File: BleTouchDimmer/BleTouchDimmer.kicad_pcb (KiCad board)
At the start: 2 copper layers, 10 parts, among them SW1 SW_PUSH, U2 MDBT40, Y2 Crystal

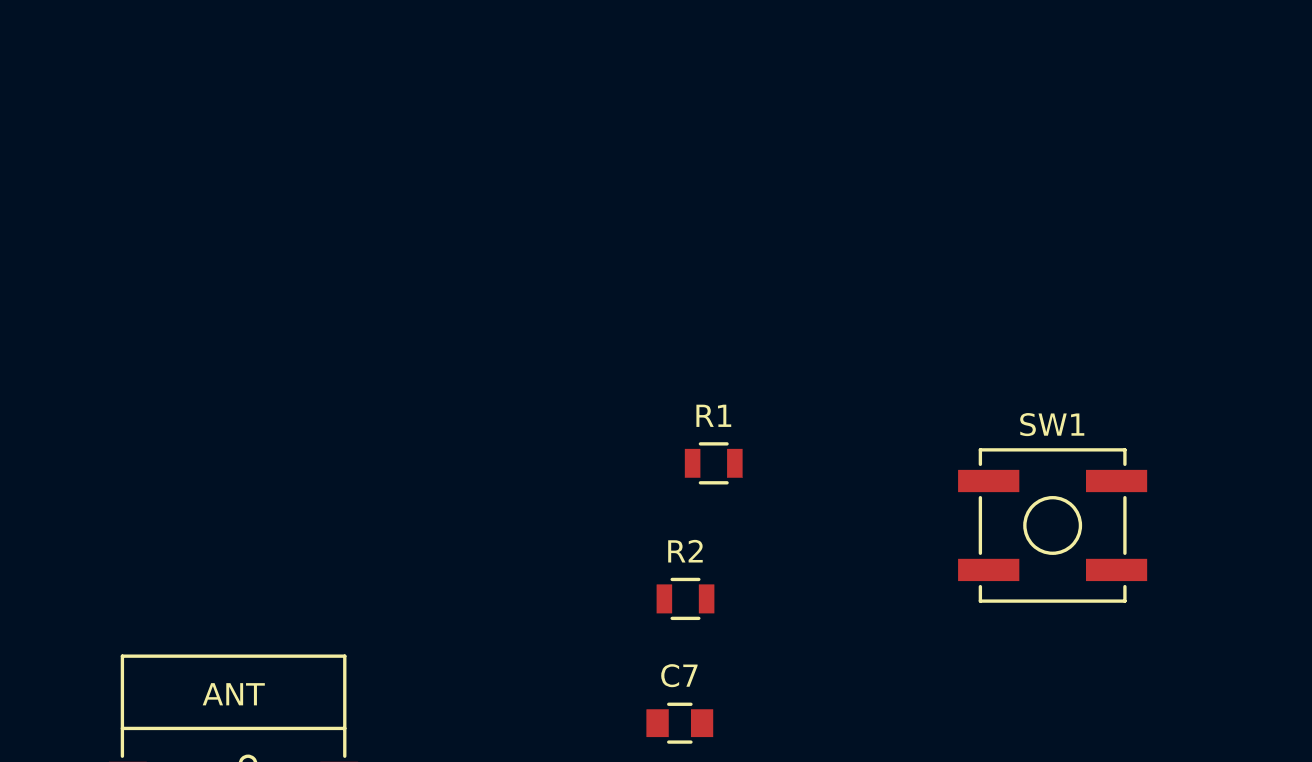
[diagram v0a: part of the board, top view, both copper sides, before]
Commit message: Started ZC_detect part. TODO select optoisolator.
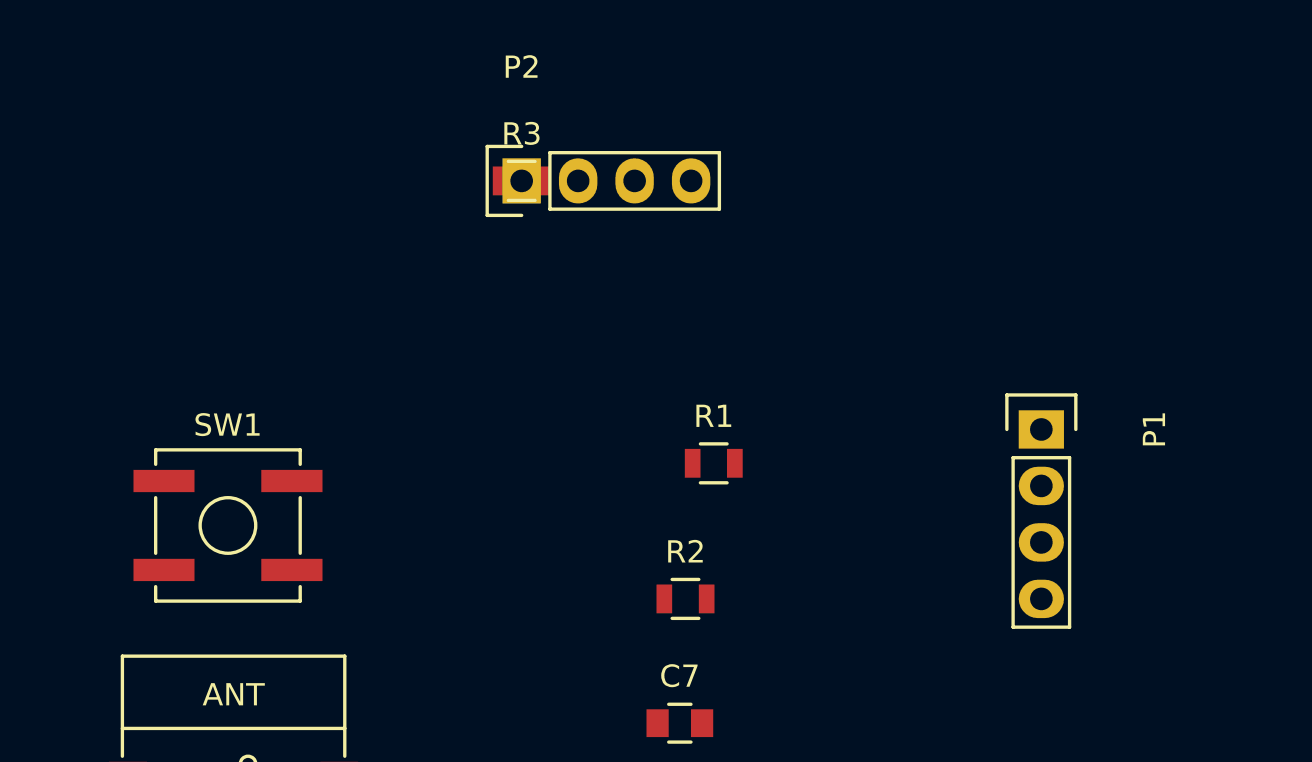
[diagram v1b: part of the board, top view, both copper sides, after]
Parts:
- added P1: PROG, Socket_Strips:Socket_Strip_Straight_1x04, F.Cu at (132.6, 60.5)
- added P2: UART, Socket_Strips:Socket_Strip_Straight_1x04, F.Cu at (109.2, 49.3)
- added R3: 10k, Resistors_SMD:R_0805, F.Cu at (109.2, 49.3)
- SW1: footprint Buttons_Switches_SMD:SW_SPST_B3SL-1002P -> Buttons_Switches_SMD:SW_SPST_B3SL-1022P
- moved SW1 37.1 mm to (96.0, 64.8)
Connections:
- U2 pad 30: (no net) -> /RX
- U2 pad 31: (no net) -> /TX
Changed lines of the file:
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@@
 (kicad_pcb (version 4) (host pcbnew 4.0.1-stable)
   (general
-    (links 25)
-    (no_connects 25)
+    (links 35)
+    (no_connects 35)
     (area 0 0 0 0)
     (thickness 1.6)
@@
     (tracks 0)
     (zones 0)
-    (modules 10)
-    (nets 7)
+    (modules 13)
+    (nets 9)
   )
   (page A4)
@@
   (net 5 /SWDIO/RESET)
   (net 6 /SWDCLK)
+  (net 7 /RX)
+  (net 8 /TX)
   (net_class Default "This is the default net class."
     (clearance 0.2)
@@
     (uvia_drill 0.1)
     (add_net +3V3)
+    (add_net /RX)
     (add_net /SWDCLK)
     (add_net /SWDIO/RESET)
+    (add_net /TX)
     (add_net GND)
     (add_net "Net-(C3-Pad2)")
@@
     (pad 28 smd rect (at 4.75 -3.2) (size 1.7 0.5) (layers F.Cu F.Paste F.Mask))
     (pad 29 smd rect (at 4.75 -3.9) (size 1.7 0.5) (layers F.Cu F.Paste F.Mask))
-    (pad 30 smd rect (at 4.75 -4.6) (size 1.7 0.5) (layers F.Cu F.Paste F.Mask))
-    (pad 31 smd rect (at 4.75 -5.3) (size 1.7 0.5) (layers F.Cu F.Paste F.Mask))
+    (pad 30 smd rect (at 4.75 -4.6) (size 1.7 0.5) (layers F.Cu F.Paste F.Mask)
+      (net 7 /RX))
+    (pad 31 smd rect (at 4.75 -5.3) (size 1.7 0.5) (layers F.Cu F.Paste F.Mask)
+      (net 8 /TX))
     (pad 32 smd rect (at 4.75 -6) (size 1.7 0.5) (layers F.Cu F.Paste F.Mask))
     (pad 33 smd rect (at 4.75 -6.7) (size 1.7 0.5) (layers F.Cu F.Paste F.Mask))
@@
     )
   )
-  (module Buttons_Switches_SMD:SW_SPST_B3SL-1002P (layer F.Cu)
-    (at 133.096 64.77)
+  (module Buttons_Switches_SMD:SW_SPST_B3SL-1022P (layer F.Cu)
+    (at 96.012 64.77)
     (descr "Middle Stroke Tactile Switch, B3SL")
     (tags "Middle Stroke Tactile Switch")
@@
       (net 1 GND))
   )
+  (module Socket_Strips:Socket_Strip_Straight_1x04 (layer F.Cu)
+    (at 132.588 60.452 270)
+    (descr "Through hole socket strip")
+    (tags "socket strip")
+    (fp_text reference P1 (at 0 -5.1 270) (layer F.SilkS)
+      (effects (font (size 1 1) (thickness 0.15)))
+    )
+    (fp_text value PROG (at 0 -3.1 270) (layer F.Fab)
+      (effects (font (size 1 1) (thickness 0.15)))
+    )
+    (fp_line (start -1.75 -1.75) (end -1.75 1.75) (layer F.CrtYd) (width 0.05))
+    (fp_line (start 9.4 -1.75) (end 9.4 1.75) (layer F.CrtYd) (width 0.05))
+    (fp_line (start -1.75 -1.75) (end 9.4 -1.75) (layer F.CrtYd) (width 0.05))
+    (fp_line (start -1.75 1.75) (end 9.4 1.75) (layer F.CrtYd) (width 0.05))
+    (fp_line (start 1.27 -1.27) (end 8.89 -1.27) (layer F.SilkS) (width 0.15))
+    (fp_line (start 1.27 1.27) (end 8.89 1.27) (layer F.SilkS) (width 0.15))
+    (fp_line (start -1.55 1.55) (end 0 1.55) (layer F.SilkS) (width 0.15))
+    (fp_line (start 8.89 -1.27) (end 8.89 1.27) (layer F.SilkS) (width 0.15))
+    (fp_line (start 1.27 1.27) (end 1.27 -1.27) (layer F.SilkS) (width 0.15))
+    (fp_line (start 0 -1.55) (end -1.55 -1.55) (layer F.SilkS) (width 0.15))
+    (fp_line (start -1.55 -1.55) (end -1.55 1.55) (layer F.SilkS) (width 0.15))
+    (pad 1 thru_hole rect (at 0 0 270) (size 1.7272 2.032) (drill 1.016) (layers *.Cu *.Mask)
+      (net 4 +3V3))
+    (pad 2 thru_hole oval (at 2.54 0 270) (size 1.7272 2.032) (drill 1.016) (layers *.Cu *.Mask)
+      (net 6 /SWDCLK))
+    (pad 3 thru_hole oval (at 5.08 0 270) (size 1.7272 2.032) (drill 1.016) (layers *.Cu *.Mask)
+      (net 5 /SWDIO/RESET))
+    (pad 4 thru_hole oval (at 7.62 0 270) (size 1.7272 2.032) (drill 1.016) (layers *.Cu *.Mask)
+      (net 1 GND))
+    (model Socket_Strips.3dshapes/Socket_Strip_Straight_1x04.wrl
+      (at (xyz 0.15 0 0))
+      (scale (xyz 1 1 1))
+      (rotate (xyz 0 0 180))
+    )
+  )
+  (module Socket_Strips:Socket_Strip_Straight_1x04 (layer F.Cu)
+    (at 109.22 49.276)
+    (descr "Through hole socket strip")
+    (tags "socket strip")
+    (fp_text reference P2 (at 0 -5.1) (layer F.SilkS)
+      (effects (font (size 1 1) (thickness 0.15)))
+    )
+    (fp_text value UART (at 0 -3.1) (layer F.Fab)
+      (effects (font (size 1 1) (thickness 0.15)))
+    )
+    (fp_line (start -1.75 -1.75) (end -1.75 1.75) (layer F.CrtYd) (width 0.05))
+    (fp_line (start 9.4 -1.75) (end 9.4 1.75) (layer F.CrtYd) (width 0.05))
+    (fp_line (start -1.75 -1.75) (end 9.4 -1.75) (layer F.CrtYd) (width 0.05))
+    (fp_line (start -1.75 1.75) (end 9.4 1.75) (layer F.CrtYd) (width 0.05))
+    (fp_line (start 1.27 -1.27) (end 8.89 -1.27) (layer F.SilkS) (width 0.15))
+    (fp_line (start 1.27 1.27) (end 8.89 1.27) (layer F.SilkS) (width 0.15))
+    (fp_line (start -1.55 1.55) (end 0 1.55) (layer F.SilkS) (width 0.15))
+    (fp_line (start 8.89 -1.27) (end 8.89 1.27) (layer F.SilkS) (width 0.15))
+    (fp_line (start 1.27 1.27) (end 1.27 -1.27) (layer F.SilkS) (width 0.15))
+    (fp_line (start 0 -1.55) (end -1.55 -1.55) (layer F.SilkS) (width 0.15))
+    (fp_line (start -1.55 -1.55) (end -1.55 1.55) (layer F.SilkS) (width 0.15))
+    (pad 1 thru_hole rect (at 0 0) (size 1.7272 2.032) (drill 1.016) (layers *.Cu *.Mask)
+      (net 4 +3V3))
+    (pad 2 thru_hole oval (at 2.54 0) (size 1.7272 2.032) (drill 1.016) (layers *.Cu *.Mask)
+      (net 7 /RX))
+    (pad 3 thru_hole oval (at 5.08 0) (size 1.7272 2.032) (drill 1.016) (layers *.Cu *.Mask)
+      (net 8 /TX))
+    (pad 4 thru_hole oval (at 7.62 0) (size 1.7272 2.032) (drill 1.016) (layers *.Cu *.Mask)
+      (net 1 GND))
+    (model Socket_Strips.3dshapes/Socket_Strip_Straight_1x04.wrl
+      (at (xyz 0.15 0 0))
+      (scale (xyz 1 1 1))
+      (rotate (xyz 0 0 180))
+    )
+  )
+  (module Resistors_SMD:R_0805 (layer F.Cu)
+    (at 109.22 49.276)
+    (descr "Resistor SMD 0805, reflow soldering, Vishay (see dcrcw.pdf)")
+    (tags "resistor 0805")
+    (attr smd)
+    (fp_text reference R3 (at 0 -2.1) (layer F.SilkS)
+      (effects (font (size 1 1) (thickness 0.15)))
+    )
+    (fp_text value 10k (at 0 2.1) (layer F.Fab)
+      (effects (font (size 1 1) (thickness 0.15)))
+    )
+    (fp_line (start -1.6 -1) (end 1.6 -1) (layer F.CrtYd) (width 0.05))
+    (fp_line (start -1.6 1) (end 1.6 1) (layer F.CrtYd) (width 0.05))
+    (fp_line (start -1.6 -1) (end -1.6 1) (layer F.CrtYd) (width 0.05))
+    (fp_line (start 1.6 -1) (end 1.6 1) (layer F.CrtYd) (width 0.05))
+    (fp_line (start 0.6 0.875) (end -0.6 0.875) (layer F.SilkS) (width 0.15))
+    (fp_line (start -0.6 -0.875) (end 0.6 -0.875) (layer F.SilkS) (width 0.15))
+    (pad 1 smd rect (at -0.95 0) (size 0.7 1.3) (layers F.Cu F.Paste F.Mask)
+      (net 7 /RX))
+    (pad 2 smd rect (at 0.95 0) (size 0.7 1.3) (layers F.Cu F.Paste F.Mask)
+      (net 4 +3V3))
+    (model Resistors_SMD.3dshapes/R_0805.wrl
+      (at (xyz 0 0 0))
+      (scale (xyz 1 1 1))
+      (rotate (xyz 0 0 0))
+    )
+  )
 )

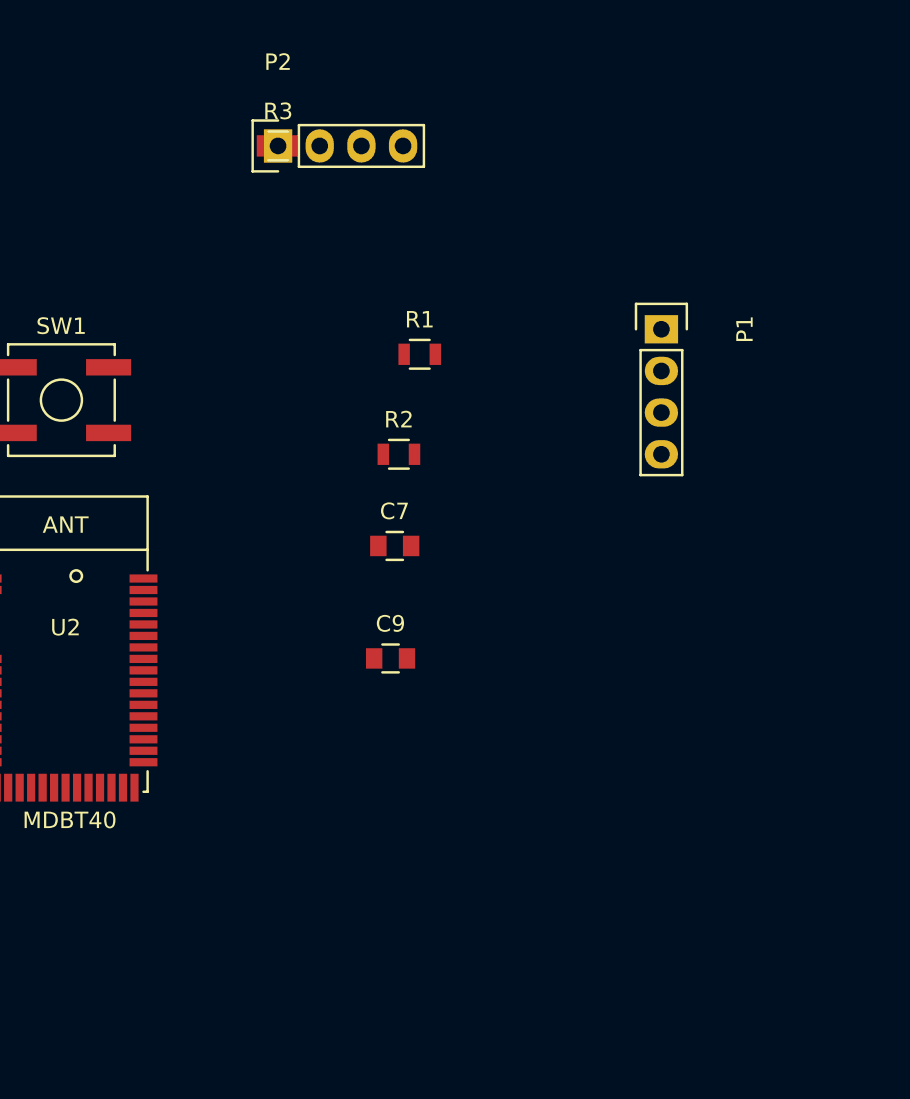
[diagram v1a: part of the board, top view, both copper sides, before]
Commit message: Started Triac logic.
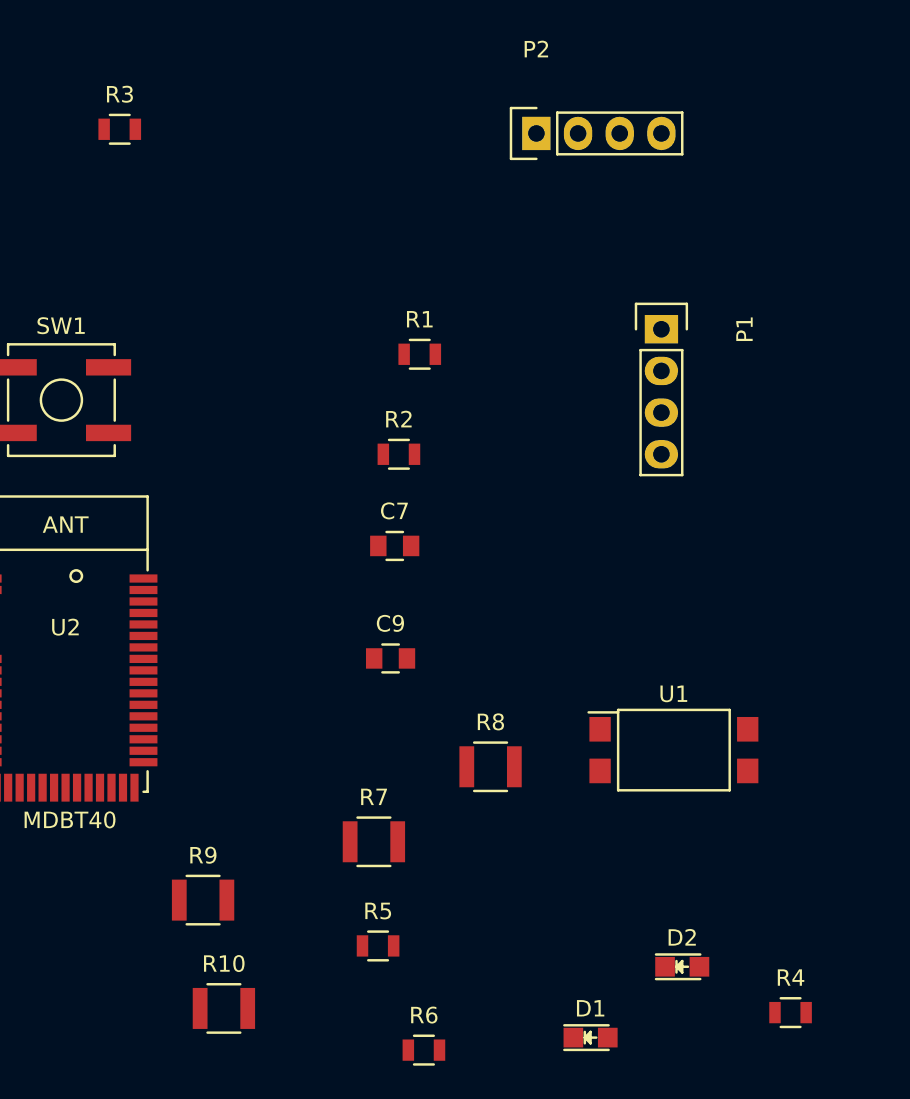
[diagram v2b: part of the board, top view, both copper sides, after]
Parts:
- added D1: LED, LEDs:LED_0805, F.Cu at (128.3, 103.6)
- added D2: LED, LEDs:LED_0805, F.Cu at (133.9, 99.3)
- added R10: 39k, Resistors_SMD:R_1210, F.Cu at (105.9, 101.9)
- added R4: 100R, Resistors_SMD:R_0805, F.Cu at (140.5, 102.1)
- added R5: 10k, Resistors_SMD:R_0805, F.Cu at (115.3, 98.0)
- added R6: 10k, Resistors_SMD:R_0805, F.Cu at (118.1, 104.4)
- added R7: 39k, Resistors_SMD:R_1210, F.Cu at (115.1, 91.7)
- added R8: 39k, Resistors_SMD:R_1210, F.Cu at (122.2, 87.1)
- added R9: 39k, Resistors_SMD:R_1210, F.Cu at (104.6, 95.2)
- added U1: LTV-814, Opto-Devices:Optocoupler_SMD_LTV-817S, F.Cu at (133.3, 86.1)
- moved P2 15.8 mm to (125.0, 48.5)
- moved R3 9.71 mm to (99.6, 48.3)
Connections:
- U2 pad 26: (no net) -> Net-(R4-Pad2)

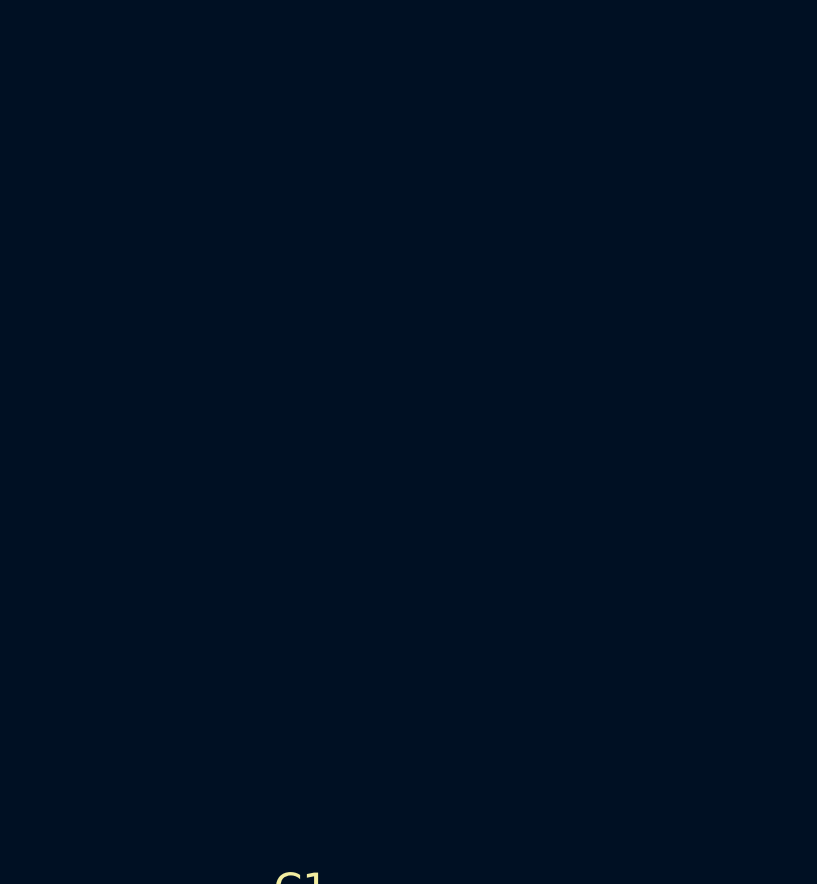
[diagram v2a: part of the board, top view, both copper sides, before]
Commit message: Changed MOC3021S footprint.
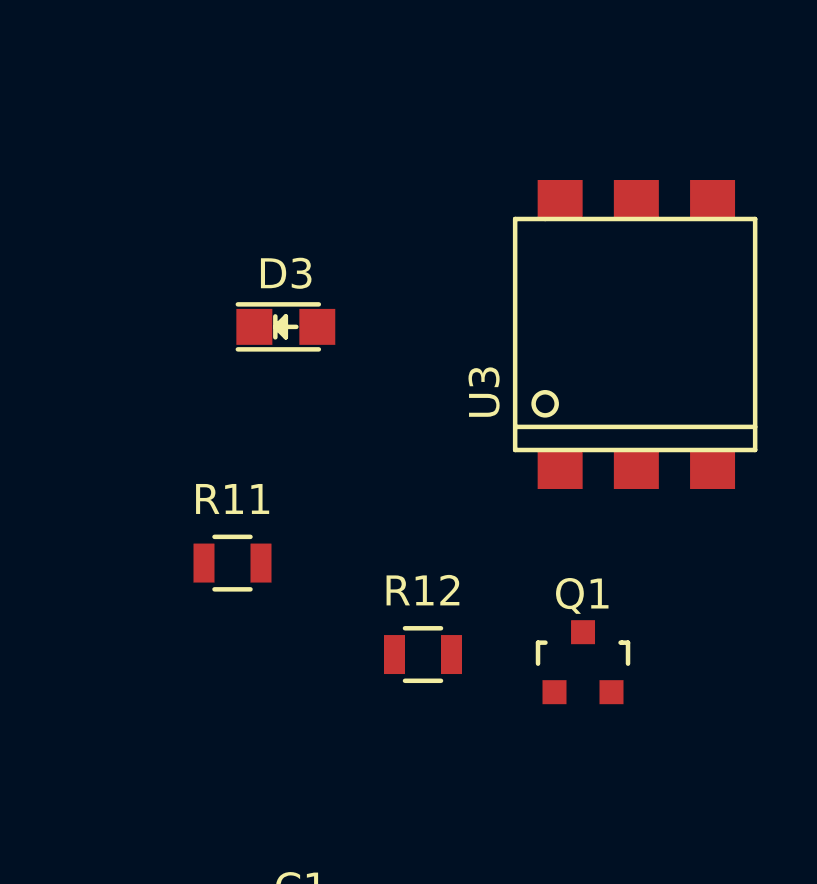
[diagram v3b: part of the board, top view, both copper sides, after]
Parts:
- added D3: LED, LEDs:LED_0805, F.Cu at (150.1, 70.9)
- added Q1: PDTC123J, TO_SOT_Packages_SMD:SOT-23, F.Cu at (160.0, 82.0)
- added R11: 100R, Resistors_SMD:R_0805, F.Cu at (148.3, 78.7)
- added R12: 220R, Resistors_SMD:R_0805, F.Cu at (154.7, 81.8)
- added U3: MOC3021S, EgertKiCad_lib:MOC3021S, F.Cu at (159.3, 71.1)
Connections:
- C1 pad 2: /SWDIO/RESET -> /Reset/SWDIO/RESET
- R2 pad 1: /SWDIO/RESET -> /Reset/SWDIO/RESET
- SW1 pad 1: /SWDIO/RESET -> /Reset/SWDIO/RESET
- U2 pad 18: (no net) -> /ZC_DETECT/ZC_DETECT
